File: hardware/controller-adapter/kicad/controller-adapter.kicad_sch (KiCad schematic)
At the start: 0 parts

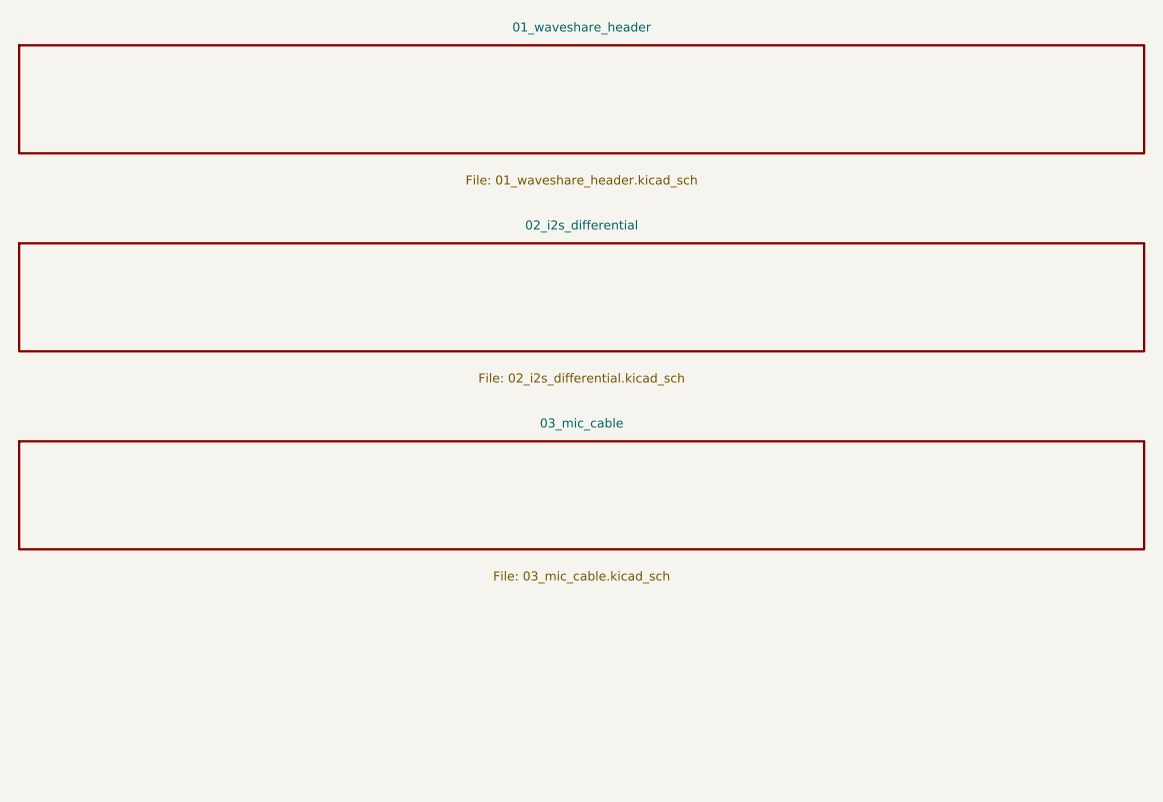
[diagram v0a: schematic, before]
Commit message: Design independent OTA recovery and update N16R8 hardware
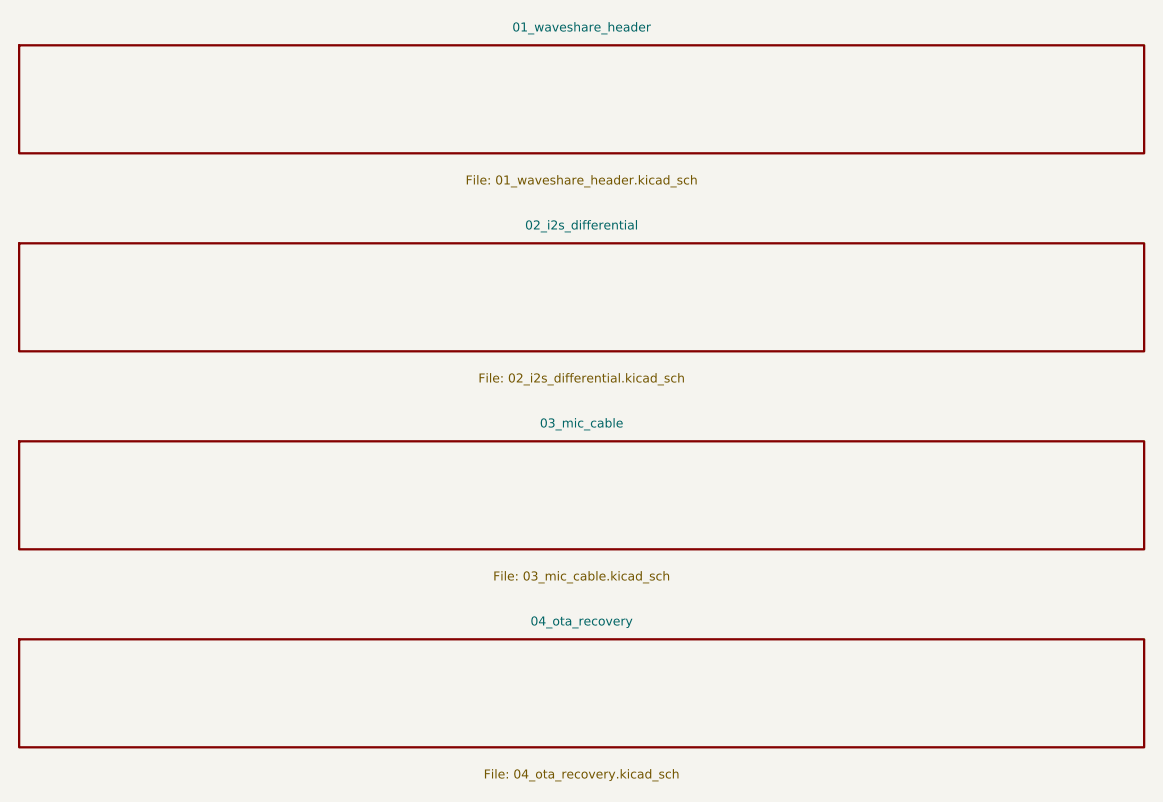
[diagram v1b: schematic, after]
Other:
- added sheet 04_ota_recovery (04_ota_recovery.kicad_sch)
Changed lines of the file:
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@@
 (sheet (at 17 52) (size 125 12) (stroke (width 0.254) (type default)) (fill (color 0 0 0 0)) (property "Sheetname" "02_i2s_differential" (at 79.5000 50.0000 0)  (effects (font (size 1.0 1.0)) )) (property "Sheetfile" "02_i2s_differential.kicad_sch" (at 79.5000 67.0000 0)  (effects (font (size 1.0 1.0)) )) (instances (project "controller-adapter" (path "/f677e06d-28c9-58b3-98b5-910baf3f6c85" (page "3")))))
 (sheet (at 17 74) (size 125 12) (stroke (width 0.254) (type default)) (fill (color 0 0 0 0)) (property "Sheetname" "03_mic_cable" (at 79.5000 72.0000 0)  (effects (font (size 1.0 1.0)) )) (property "Sheetfile" "03_mic_cable.kicad_sch" (at 79.5000 89.0000 0)  (effects (font (size 1.0 1.0)) )) (instances (project "controller-adapter" (path "/f677e06d-28c9-58b3-98b5-910baf3f6c85" (page "4")))))
+(sheet (at 17 96) (size 125 12) (stroke (width 0.254) (type default)) (fill (color 0 0 0 0)) (property "Sheetname" "04_ota_recovery" (at 79.5000 94.0000 0)  (effects (font (size 1.0 1.0)) )) (property "Sheetfile" "04_ota_recovery.kicad_sch" (at 79.5000 111.0000 0)  (effects (font (size 1.0 1.0)) )) (instances (project "controller-adapter" (path "/f677e06d-28c9-58b3-98b5-910baf3f6c85" (page "5")))))
 (sheet_instances (path "/" (page "1")))
 )
